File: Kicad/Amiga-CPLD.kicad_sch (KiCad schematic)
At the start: 19 parts, among them CN1 CDTV-DIAG, J1 JTAG, SW1 SW_DIP_x04, U1 AZ1117-3.3, U2 XC95144XL-TQ100, X1 50MHz

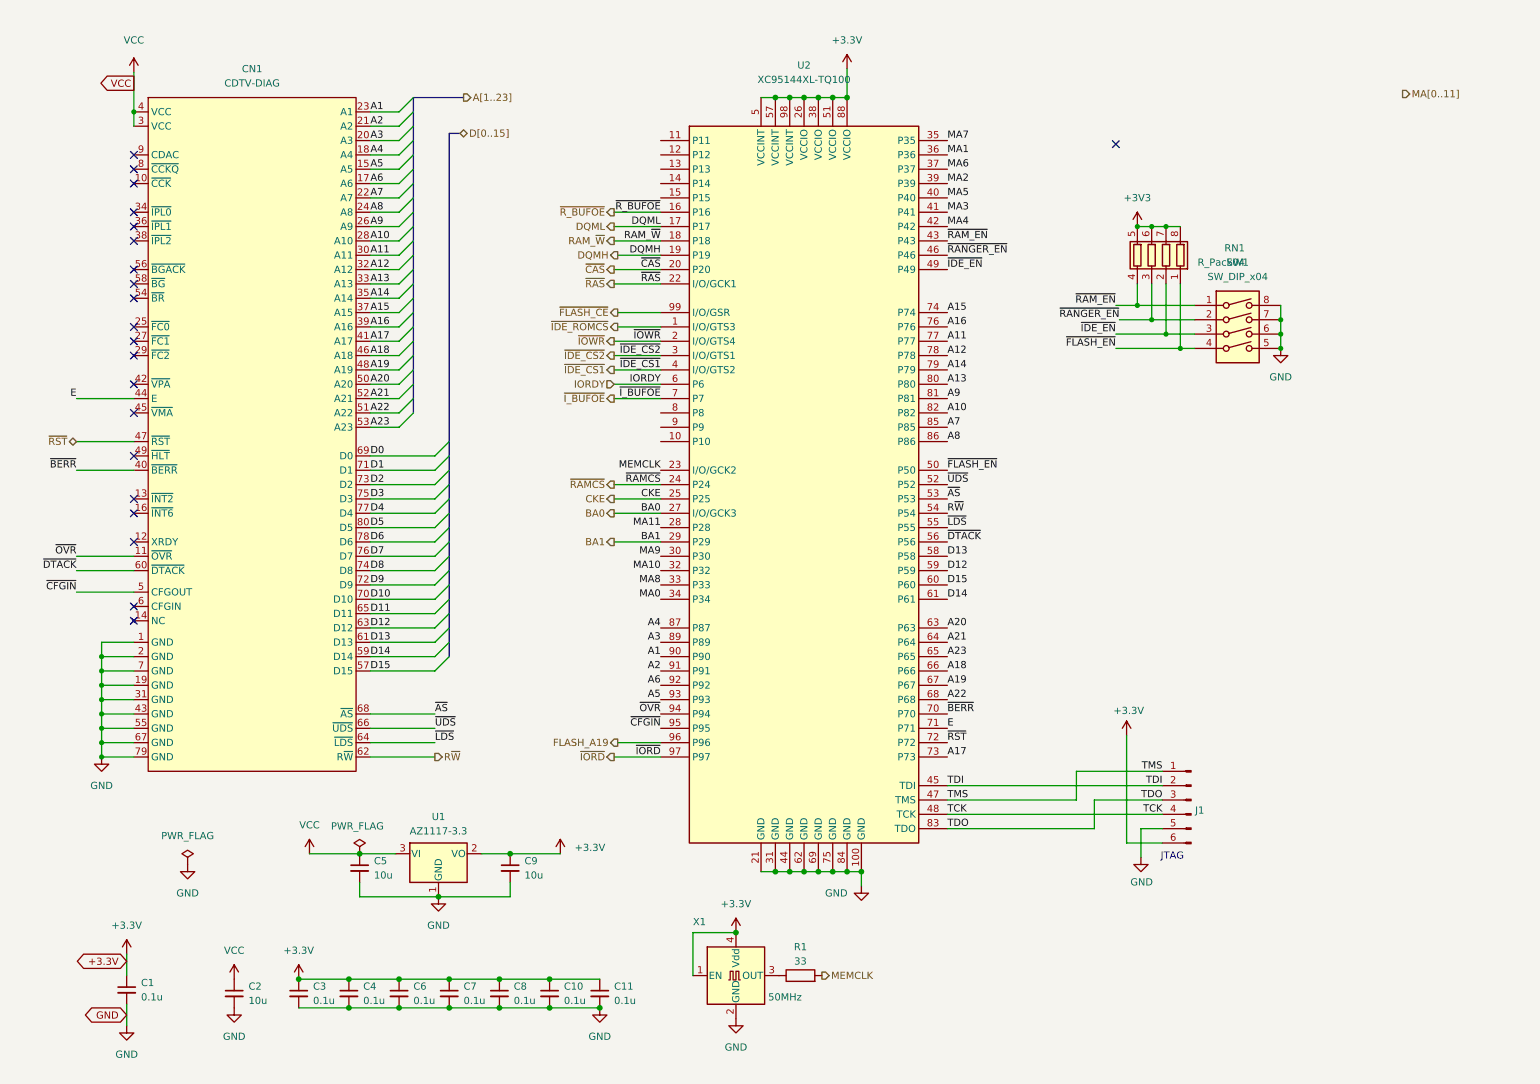
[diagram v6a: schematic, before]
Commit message: PCB: Route Flash bank switch jumper
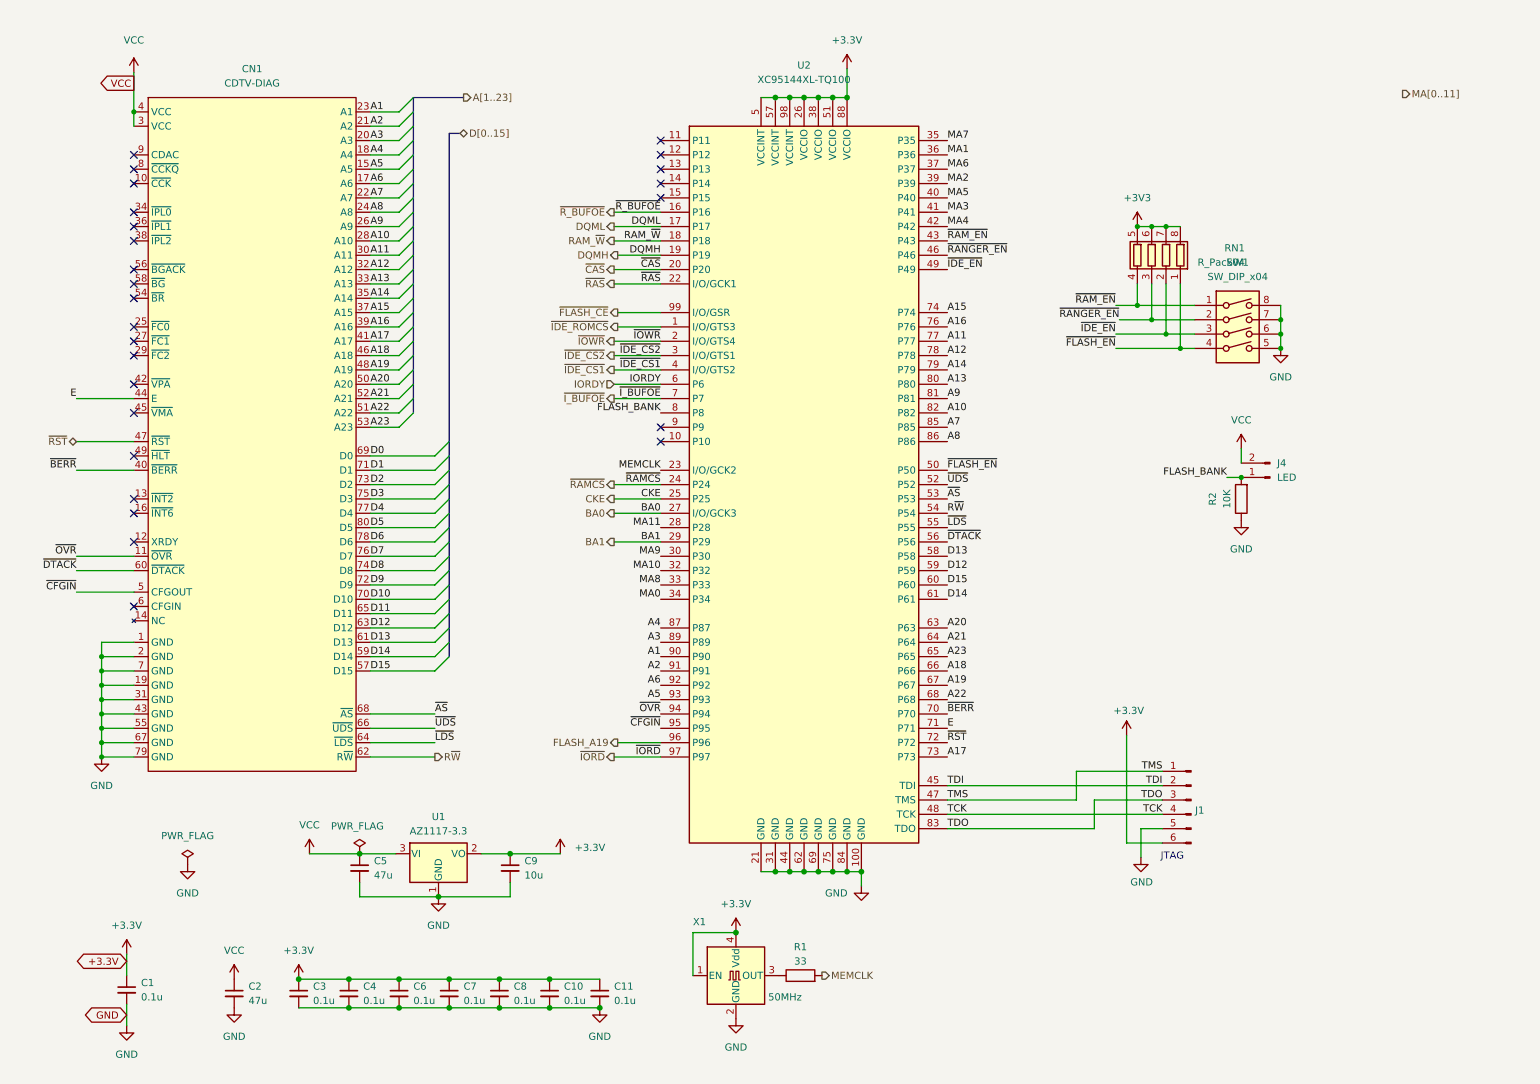
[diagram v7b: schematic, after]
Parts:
- added J4: LED, Connector_PinHeader_2.00mm:PinHeader_1x02_P2.00mm_Vertical, symbol Connector:Conn_01x02_Male
- added R2: 10K, Resistor_SMD:R_0603_1608Metric, symbol Device:R
- C2, C5: value 10u -> 47u; LCSC # C117023 -> C193224
- C9: LCSC # C117023 -> C7171
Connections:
- net GND: now also R2.1
- net VCC: now also J4.2 (Pin_2)
- net FLASH_BANK: now reaches U2.8 (P8)
- net FLASH_BANK: now also J4.1 (Pin_1), R2.2
- no-connect marks 21 -> 26
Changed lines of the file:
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@@
   (junction (at 95.885 180.34) (diameter 1.016) (color 0 0 0 0)
   )
+  (junction (at 236.22 91.44) (diameter 0) (color 0 0 0 0)
+  )
   (junction (at 78.105 180.34) (diameter 1.016) (color 0 0 0 0)
   )
@@
   (junction (at 86.995 180.34) (diameter 1.016) (color 0 0 0 0)
   )
-  (no_connect (at 213.995 32.385))
   (no_connect (at 40.005 39.37))
   (no_connect (at 40.005 44.45))
@@
   (no_connect (at 40.005 46.99))
   (no_connect (at 40.005 49.53))
-  (no_connect (at 40.005 116.84))
+  (no_connect (at 133.35 31.75))
+  (no_connect (at 133.35 34.29))
+  (no_connect (at 133.35 36.83))
+  (no_connect (at 133.35 39.37))
+  (no_connect (at 133.35 41.91))
+  (no_connect (at 133.35 82.55))
+  (no_connect (at 133.35 85.09))
   (no_connect (at 40.005 97.79))
   (no_connect (at 40.005 102.87))
@@
     (stroke (width 0) (type default) (color 0 0 0 0))
   )
+  (wire (pts (xy 236.22 86.36) (xy 236.22 88.9))
+    (stroke (width 0) (type default) (color 0 0 0 0))
+  )
   (wire (pts (xy 71.12 158.115) (xy 80.01 158.115))
     (stroke (width 0) (type solid) (color 0 0 0 0))
@@
     (stroke (width 0) (type solid) (color 0 0 0 0))
   )
+  (wire (pts (xy 233.68 91.44) (xy 236.22 91.44))
+    (stroke (width 0) (type default) (color 0 0 0 0))
+  )
   (wire (pts (xy 133.35 69.85) (xy 125.095 69.85))
     (stroke (width 0) (type default) (color 0 0 0 0))
@@
     (effects (font (size 1.27 1.27)) (justify left bottom))
   )
+  (label "FLASH_BANK" (at 133.35 80.01 180)
+    (effects (font (size 1.27 1.27)) (justify right bottom))
+  )
   (label "TCK" (at 184.15 151.13 0)
     (effects (font (size 1.27 1.27)) (justify left bottom))
@@
   (label "~{RAM_EN}" (at 184.15 49.53 0)
     (effects (font (size 1.27 1.27)) (justify left bottom))
+  )
+  (label "FLASH_BANK" (at 233.68 91.44 180)
+    (effects (font (size 1.27 1.27)) (justify right bottom))
   )
   (label "~{DTACK}" (at 29.845 107.95 180)
@@
       (effects (font (size 1.27 1.27)) hide)
     )
-    (property "LCSC #" "C117023" (id 4) (at 106.68 160.655 0)
+    (property "LCSC #" "C7171" (id 4) (at 106.68 160.655 0)
       (effects (font (size 1.27 1.27)) hide)
     )
@@
     (pin "1")
   )
+  (symbol (lib_id "power:VCC") (at 236.22 86.36 0) (unit 1)
+    (in_bom yes) (on_board yes) (fields_autoplaced)
+    (property "Reference" "#PWR08" (id 0) (at 236.22 90.17 0)
+      (effects (font (size 1.27 1.27)) hide)
+    )
+    (property "Value" "VCC" (id 1) (at 236.22 81.28 0))
+    (property "Footprint" "" (id 2) (at 236.22 86.36 0)
+      (effects (font (size 1.27 1.27)) hide)
+    )
+    (property "Datasheet" "" (id 3) (at 236.22 86.36 0)
+      (effects (font (size 1.27 1.27)) hide)
+    )
+    (pin "1")
+  )
   (symbol (lib_id "Device:C_Small") (at 57.785 182.88 0) (unit 1)
     (in_bom yes) (on_board yes) (fields_autoplaced)
@@
       (effects (font (size 1.27 1.27)) (justify left))
     )
-    (property "Value" "10u" (id 1) (at 60.325 184.1499 0)
+    (property "Value" "47u" (id 1) (at 60.325 184.1499 0)
       (effects (font (size 1.27 1.27)) (justify left))
     )
@@
       (effects (font (size 1.27 1.27)) hide)
     )
-    (property "LCSC #" "C117023" (id 4) (at 57.785 182.88 0)
+    (property "LCSC #" "C193224" (id 4) (at 57.785 182.88 0)
       (effects (font (size 1.27 1.27)) hide)
     )
@@
     (pin "6")
   )
+  (symbol (lib_id "power:GND") (at 236.22 99.06 0) (unit 1)
+    (in_bom yes) (on_board yes) (fields_autoplaced)
+    (property "Reference" "#PWR019" (id 0) (at 236.22 105.41 0)
+      (effects (font (size 1.27 1.27)) hide)
+    )
+    (property "Value" "GND" (id 1) (at 236.22 104.14 0))
+    (property "Footprint" "" (id 2) (at 236.22 99.06 0)
+      (effects (font (size 1.27 1.27)) hide)
+    )
+    (property "Datasheet" "" (id 3) (at 236.22 99.06 0)
+      (effects (font (size 1.27 1.27)) hide)
+    )
+    (pin "1")
+  )
   (symbol (lib_id "Device:C_Small") (at 80.01 160.655 0) (unit 1)
     (in_bom yes) (on_board yes) (fields_autoplaced)
@@
       (effects (font (size 1.27 1.27)) (justify left))
     )
-    (property "Value" "10u" (id 1) (at 82.55 161.9249 0)
+    (property "Value" "47u" (id 1) (at 82.55 161.9249 0)
       (effects (font (size 1.27 1.27)) (justify left))
     )
@@
       (effects (font (size 1.27 1.27)) hide)
     )
-    (property "LCSC #" "C117023" (id 4) (at 80.01 160.655 0)
+    (property "LCSC #" "C193224" (id 4) (at 80.01 160.655 0)
       (effects (font (size 1.27 1.27)) hide)
     )
@@
     (pin "1")
   )
+  (symbol (lib_id "Device:R") (at 236.22 95.25 180) (unit 1)
+    (in_bom yes) (on_board yes)
+    (property "Reference" "R2" (id 0) (at 231.14 95.25 90))
+    (property "Value" "10K" (id 1) (at 233.68 95.25 90))
+    (property "Footprint" "Resistor_SMD:R_0603_1608Metric" (id 2) (at 237.998 95.25 90)
+      (effects (font (size 1.27 1.27)) hide)
+    )
+    (property "Datasheet" "~" (id 3) (at 236.22 95.25 0)
+      (effects (font (size 1.27 1.27)) hide)
+    )
+    (property "LCSC #" "C25804" (id 4) (at 236.22 95.25 90)
+      (effects (font (size 1.27 1.27)) hide)
+    )
+    (pin "1")
+    (pin "2")
+  )
   (symbol (lib_id "Oscillator:ASE-xxxMHz") (at 146.685 179.705 0) (unit 1)
     (in_bom yes) (on_board yes)
@@
     (pin "4")
   )
+  (symbol (lib_id "Connector:Conn_01x02_Male") (at 241.3 91.44 180) (unit 1)
+    (in_bom yes) (on_board yes) (fields_autoplaced)
+    (property "Reference" "J4" (id 0) (at 242.57 88.8999 0)
+      (effects (font (size 1.27 1.27)) (justify right))
+    )
+    (property "Value" "LED" (id 1) (at 242.57 91.4399 0)
+      (effects (font (size 1.27 1.27)) (justify right))
+    )
+    (property "Footprint" "Connector_PinHeader_2.00mm:PinHeader_1x02_P2.00mm_Vertical" (id 2) (at 241.3 91.44 0)
+      (effects (font (size 1.27 1.27)) hide)
+    )
+    (property "Datasheet" "~" (id 3) (at 241.3 91.44 0)
+      (effects (font (size 1.27 1.27)) hide)
+    )
+    (pin "1")
+    (pin "2")
+  )
   (symbol (lib_id "Switch:SW_DIP_x04") (at 235.585 66.04 0) (unit 1)

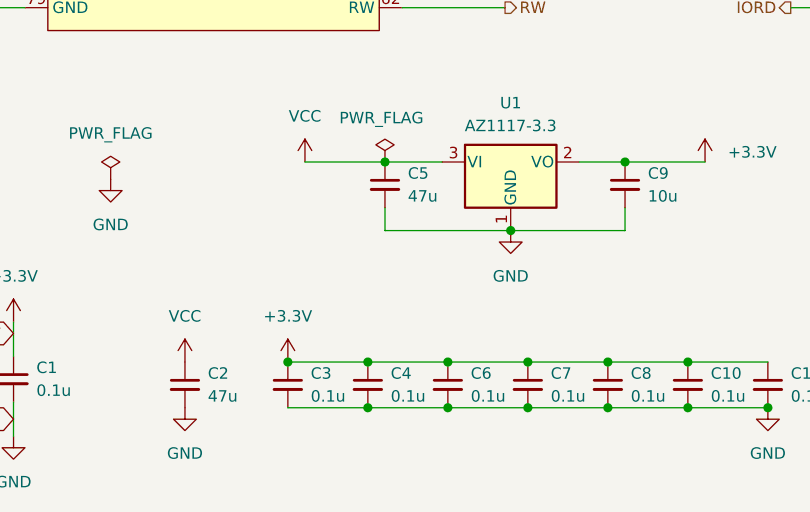
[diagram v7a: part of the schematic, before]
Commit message: PCB: Add 22 Ohm series resistors for SDRAM
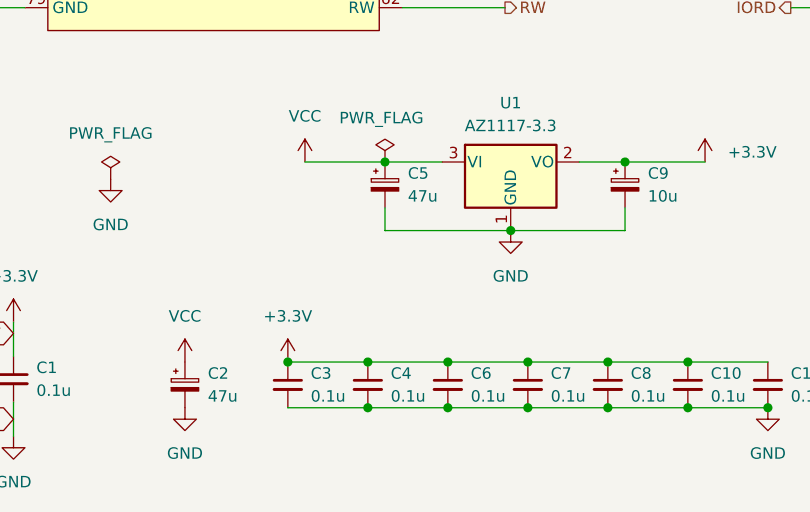
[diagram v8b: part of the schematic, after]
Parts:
- C2, C5, C9: symbol Device:C_Small -> Device:C_Polarized_Small
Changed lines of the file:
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@@
     (pin "1")
   )
-  (symbol (lib_id "Device:C_Small") (at 106.68 160.655 0) (unit 1)
+  (symbol (lib_id "Device:C_Polarized_Small") (at 106.68 160.655 0) (unit 1)
     (in_bom yes) (on_board yes) (fields_autoplaced)
     (property "Reference" "C9" (id 0) (at 109.22 159.3849 0)
@@
     (pin "1")
   )
-  (symbol (lib_id "Device:C_Small") (at 57.785 182.88 0) (unit 1)
+  (symbol (lib_id "Device:C_Polarized_Small") (at 57.785 182.88 0) (unit 1)
     (in_bom yes) (on_board yes) (fields_autoplaced)
     (property "Reference" "C2" (id 0) (at 60.325 181.6099 0)
@@
     (pin "1")
   )
-  (symbol (lib_id "Device:C_Small") (at 80.01 160.655 0) (unit 1)
+  (symbol (lib_id "Device:C_Polarized_Small") (at 80.01 160.655 0) (unit 1)
     (in_bom yes) (on_board yes) (fields_autoplaced)
     (property "Reference" "C5" (id 0) (at 82.55 159.3849 0)
